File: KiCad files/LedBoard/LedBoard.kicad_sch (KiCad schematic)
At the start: 21 parts, among them J4 7-5530843-7

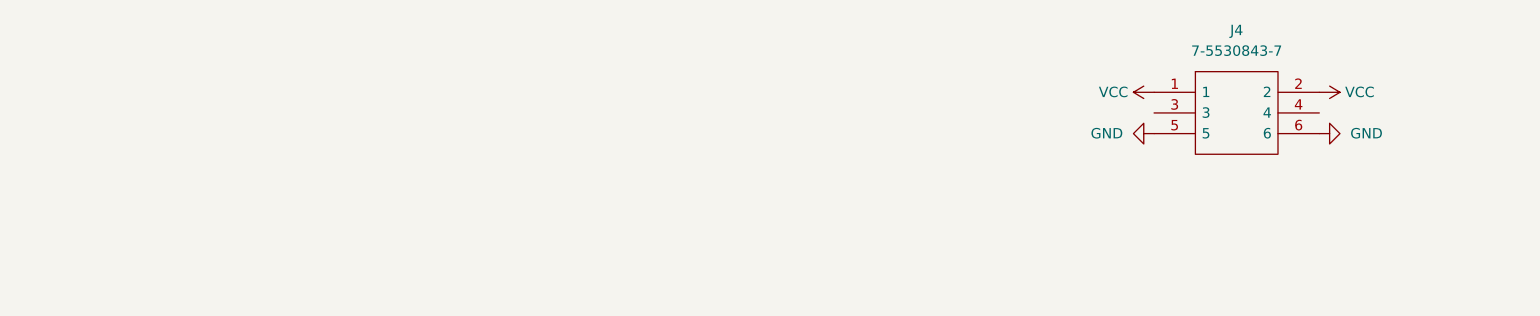
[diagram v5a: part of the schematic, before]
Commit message: made some adjustments to improve design reliability.
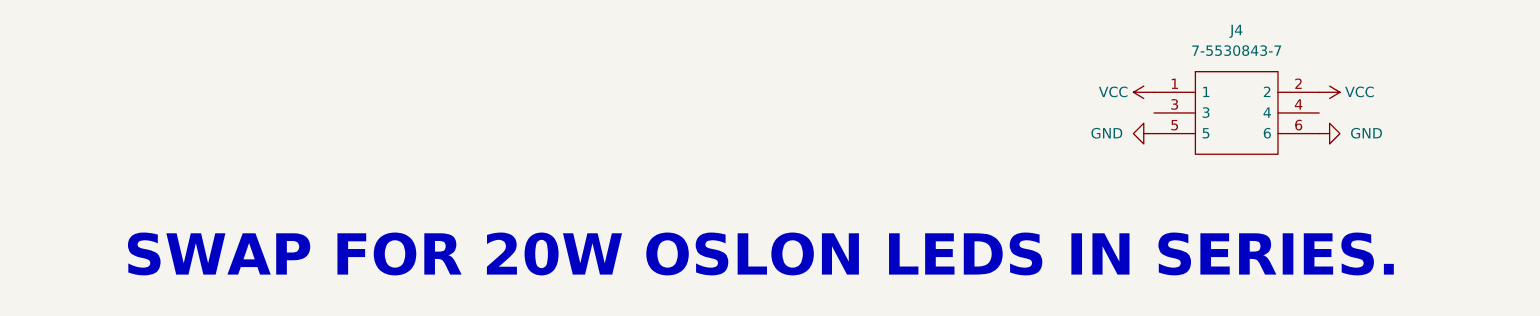
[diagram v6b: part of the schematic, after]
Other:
- note added: "SWAP FOR 20W OSLON LEDS IN SERIES."
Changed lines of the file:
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@@
+		)
+	)
+	(text "SWAP FOR 20W OSLON LEDS IN SERIES."
+		(exclude_from_sim no)
+		(at 97.79 123.19 0)
+		(effects
+			(font
+				(size 5.08 5.08)
+				(thickness 1.016)
+				(bold yes)
+			)
 		)
 	)
